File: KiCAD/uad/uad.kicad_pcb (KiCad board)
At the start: 2 copper layers, 100 x 70 mm, 58 parts, among them M3 ОтверстиеD3

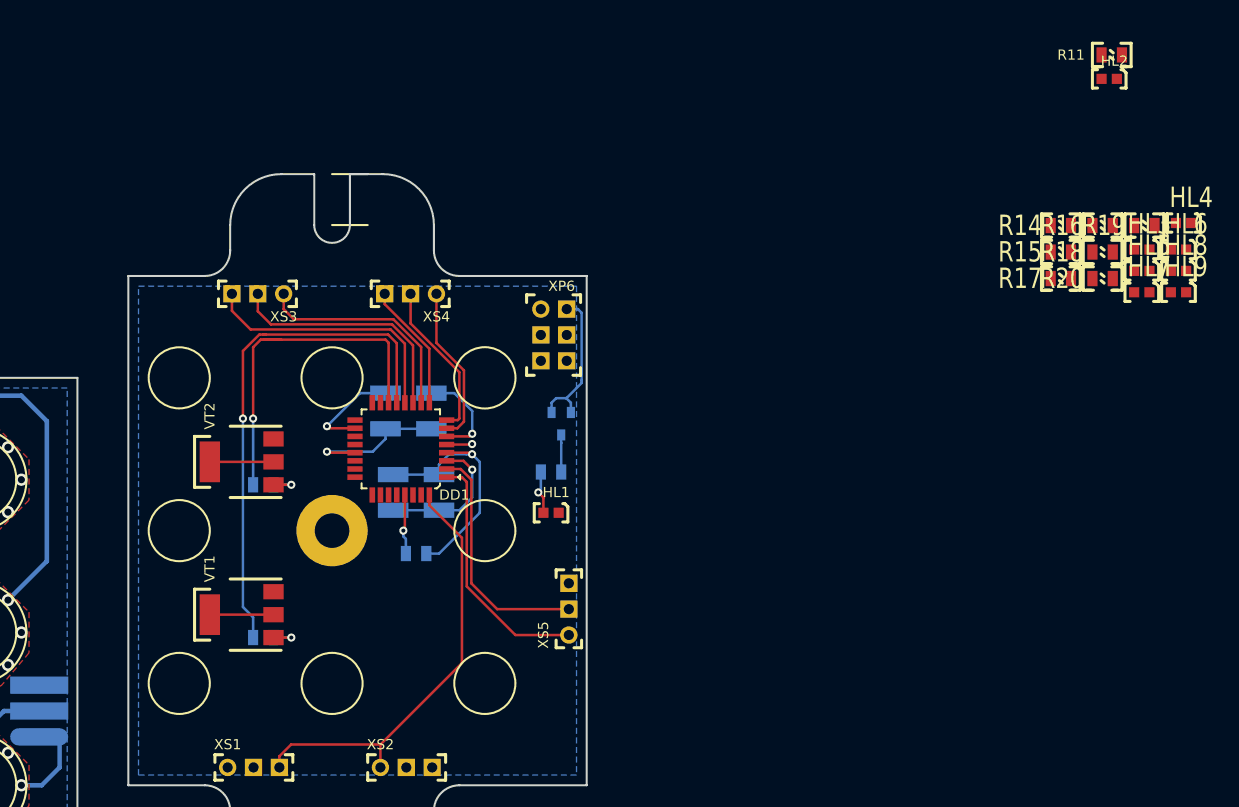
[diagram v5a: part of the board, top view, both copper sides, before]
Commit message: не поставлен эмиттерный повторитель на питание логики
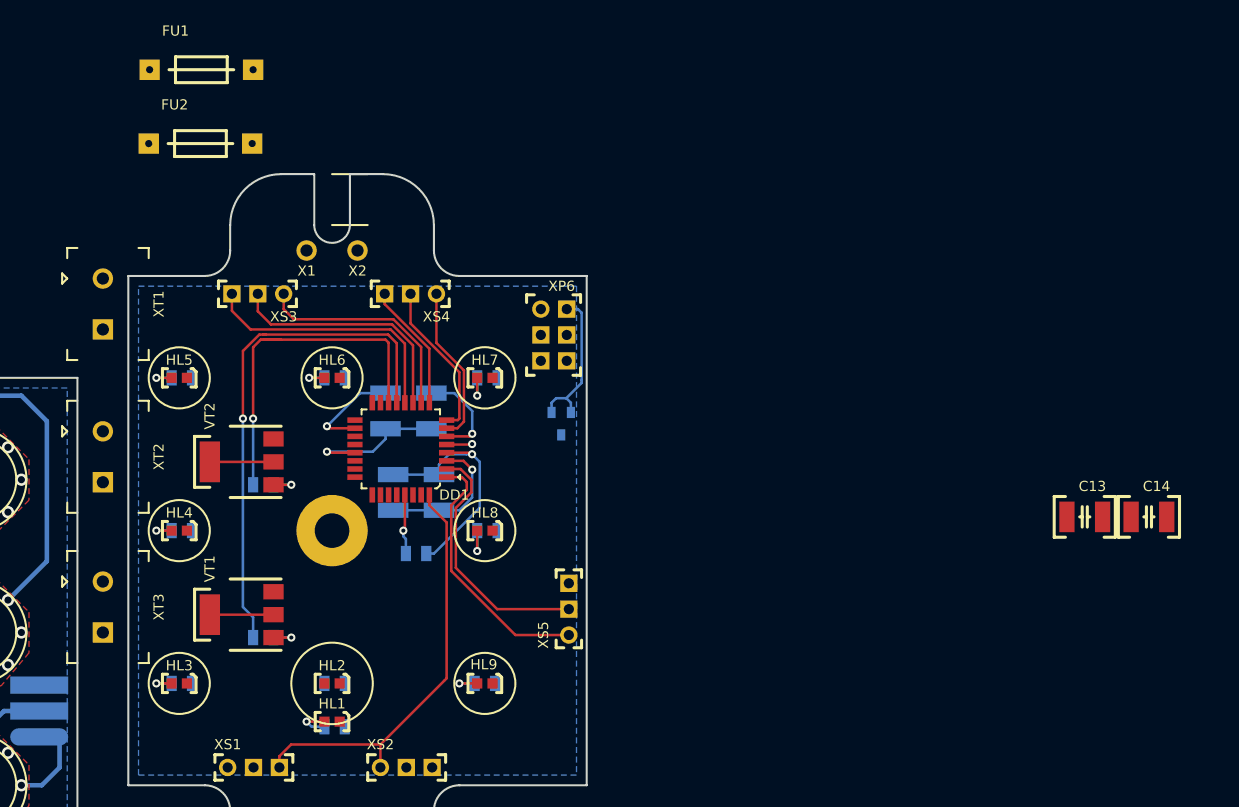
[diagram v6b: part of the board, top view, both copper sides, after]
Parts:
- added C13: 4.7мкФ(1210), N_RLC:Конденсатор_SMD_1210, F.Cu at (217.4, 111.7)
- added C14: 4.7мкФ(1210), N_RLC:Конденсатор_SMD_1210, F.Cu at (223.7, 111.7)
- added FU1: Предохранитель, N_RLC:Предохранитель_R700, F.Cu at (127.3, 67.8)
- added FU2: Предохранитель, N_RLC:Предохранитель_R700, F.Cu at (127.2, 75.0)
- added X1: L_220, N_X:ОтверстиеD1.2, F.Cu at (142.8, 85.5)
- added X2: N_220, N_X:ОтверстиеD1.2, F.Cu at (147.8, 85.5)
- added XT1: Клеммник_х2, N_X:Клеммник_х2_шаг5, F.Cu at (122.8, 88.2)
- added XT2: Клеммник_х2, N_X:Клеммник_х2_шаг5, F.Cu at (122.8, 103.2)
- added XT3: Клеммник_х2, N_X:Клеммник_х2_шаг5, F.Cu at (122.8, 118.0)
- R11, R14, R15, R16, R17, R18, R19, R20: moved to B.Cu
- moved HL3 103.7 mm to (129.5, 128.0)
- moved HL4 103.1 mm to (129.5, 113.0)
- moved HL2 96.7 mm to (144.5, 128.0)
- moved R11 96.6 mm to (146.5, 128.0), turned to 180 degrees
- moved R14 95.5 mm to (131.5, 128.0), turned to 180 degrees
- moved HL5 95.1 mm to (129.5, 98.0)
- moved R16 89.7 mm to (131.5, 98.0), turned to 180 degrees
- moved R15 88.6 mm to (131.5, 113.0), turned to 180 degrees
- moved HL6 84.0 mm to (144.5, 98.0)
- moved HL9 78.2 mm to (159.5, 128.0)
- moved HL8 72.7 mm to (159.5, 113.0)
- moved R20 70.9 mm to (161.2, 128.0), turned to 180 degrees
- moved R17 70.0 mm to (146.5, 98.0), turned to 180 degrees
- moved R19 69.3 mm to (161.5, 113.0), turned to 180 degrees
- moved HL7 65.0 mm to (159.5, 98.0)
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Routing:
- net Net-(HL8-Pad1): track 0.00 -> 4.00 mm, vias 0 -> 1
- net /uab_logic/VCC: track 47.9 -> 43.9 mm
- net Net-(HL7-Pad1): track 0.00 -> 3.50 mm, vias 0 -> 1
- net Net-(HL9-Pad1): track 0.00 -> 3.25 mm, vias 0 -> 1
- net Net-(HL6-Pad1): track 0.00 -> 3.00 mm, vias 0 -> 1
- net Net-(HL5-Pad1): track 0.00 -> 3.00 mm, vias 0 -> 1
- net Net-(HL4-Pad1): track 0.00 -> 3.00 mm, vias 0 -> 1
- net Net-(HL3-Pad1): track 0.00 -> 3.00 mm, vias 0 -> 1
- net /uab_logic/BUT_8_IN: track 24.4 -> 25.7 mm
- net /uab_logic/BUT_1_IN: track 23.7 -> 24.9 mm
- net /uab_logic/BUT_COM_OUT: track 42.9 -> 41.6 mm
- net Net-(HL1-Pad1): track 4.31 -> 3.71 mm

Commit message: обе схемы закончены, разводка второй платы не закончена
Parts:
- added C15: 4.7мкФ(1210), N_RLC:Конденсатор_SMD_1210, F.Cu at (198.0, 73.2)
- added G1: Стабилиатор_LM2931AZ-5.0G, N_G:Стабилизатор_корпус_TO-92, F.Cu at (233.1, 81.9)
- added L1: 33мкГн, N_RLC:Чип-индуктивность_SMD_0805, F.Cu at (231.5, 93.8)
- added L2: 33мкГн, N_RLC:Чип-индуктивность_SMD_0805, F.Cu at (247.2, 81.0)
- added L3: 33мкГн, N_RLC:Чип-индуктивность_SMD_0805, F.Cu at (242.5, 93.8)
- added VD2: Мост_DB155S, N_VD_HL:Диод_матрица_корпус_DB-1S, B.Cu at (153.2, 132.0)
- added VD3: Шоттки_BAR43CFILM, N_VD_HL:Диод_BAR43CFILM_SOT-23, F.Cu at (253.5, 89.8)
- added X3: L_12, N_X:ОтверстиеD1.2, F.Cu at (147.8, 140.0)
- added X4: N_12, N_X:ОтверстиеD1.2, F.Cu at (142.8, 140.0)
- FU1, FU2: footprint N_RLC:Предохранитель_R700 -> N_RLC:Предохранитель_MF-R_d10.4; moved to B.Cu
- VD1: value Диод_шоттки -> Шоттки_BAR43CFILM
- XT1, XT2, XT3: footprint N_X:Клеммник_х2_шаг5 -> N_X:Клеммник_х2_шаг2.54
- moved FU2 69.6 mm to (162.5, 135.0), turned to 45 degrees
- moved FU1 52.1 mm to (167.5, 101.0), turned to 90 degrees
- moved XT1 47.1 mm to (166.0, 107.0), turned to 90 degrees
- moved VD1 30.0 mm to (197.7, 101.6)
- moved XP6 29.8 mm to (195.5, 91.0)
- moved XT2 16.2 mm to (126.5, 119.0)
- moved XT3 14.0 mm to (126.5, 104.5)
- moved C1 10.2 mm to (95.2, 136.2)
- moved C2 10.2 mm to (80.2, 136.2)
- moved C3 10.2 mm to (80.2, 121.2)
- moved C4 10.2 mm to (80.2, 106.2)
- moved C5 10.2 mm to (95.2, 106.2)
- moved C6 10.2 mm to (110.2, 106.2)
- moved C8 10.2 mm to (110.2, 136.2)
- moved C7 10.1 mm to (110.2, 121.2)
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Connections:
- net Net-(FU1-Pad2) renamed /uab_logic/L2
- DD1 pad 1: /uab_logic/BUT_8_IN -> /uab_logic/LED_7
- DD1 pad 15: /uab_logic/MOSI -> /uab_logic/LED_5
- DD1 pad 16: /uab_logic/MISO -> /uab_logic/LED_4
- DD1 pad 2: /uab_logic/BUT_1_IN -> /uab_logic/LED_6
- DD1 pad 23: Net-(DD1-Pad23) -> /uab_logic/LED_3
- DD1 pad 24: Net-(DD1-Pad24) -> /uab_logic/LED_2
- DD1 pad 25: Net-(DD1-Pad25) -> /uab_logic/LED_1
- DD1 pad 26: Net-(DD1-Pad26) -> /uab_logic/BUT_COM_OUT
- DD1 pad 27: Net-(DD1-Pad27) -> /uab_logic/LED_8
- DD1 pad 28: Net-(DD1-Pad28) -> /uab_logic/BUT_8_IN
- DD1 pad 32: /uab_logic/BUT_COM_OUT -> /uab_logic/BUT_1_IN
- FU1 pad 1: Net-(FU1-Pad1) -> /uab_logic/L1
- FU2 pad 1: Net-(FU2-Pad1) -> /uab_logic/L1_12
- FU2 pad 2: Net-(FU2-Pad2) -> /uab_logic/L2_12
- X2 pad 1: Net-(FU2-Pad2) -> /uab_logic/N1
- XP6 pad 1: /uab_logic/MISO -> /uab_logic/LED_4
- XP6 pad 4: /uab_logic/MOSI -> /uab_logic/LED_5
- XT1 pad 1: Net-(FU1-Pad1) -> /uab_logic/N1
- XT1 pad 2: Net-(FU2-Pad1) -> /uab_logic/L1
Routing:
- net /uab_logic/N1: track 0.00 -> 41.5 mm
- net /uab_logic/LED_2: track 0.00 -> 34.1 mm, vias 0 -> 1
- net /uab_logic/N1_12: track 0.00 -> 27.5 mm
- net /uab_logic/PWM_OUT_1: track 50.8 -> 24.1 mm
- net /uab_logic/L2: track 0.00 -> 24.4 mm
- net /uab_logic/LED_8: track 0.00 -> 21.6 mm, vias 0 -> 1
- net /uab_logic/LED_1: track 0.00 -> 20.0 mm, vias 0 -> 1
- net /uab_logic/LED_4: track 0.00 -> 19.9 mm, vias 0 -> 1
- net /uab_logic/LED_3: track 0.00 -> 18.5 mm, vias 0 -> 1
- net /uab_logic/L1_12: track 0.00 -> 16.8 mm
- net /uab_logic/LED_6: track 0.00 -> 16.7 mm, vias 0 -> 1
- net Net-(VD1-Pad1): track 14.8 -> 0.00 mm
- net /uab_logic/PWM_OUT_2: track 34.9 -> 22.1 mm
- net /uab_logic/LED_7: track 0.00 -> 11.2 mm, vias 0 -> 1
- net /uab_logic/LED_5: track 0.00 -> 5.66 mm, vias 0 -> 1
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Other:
- outline, holes or cut-outs redrawn
- net class power added: clearance 0.4, trace_width 0.45, via_dia 0.8, via_drill 0.4

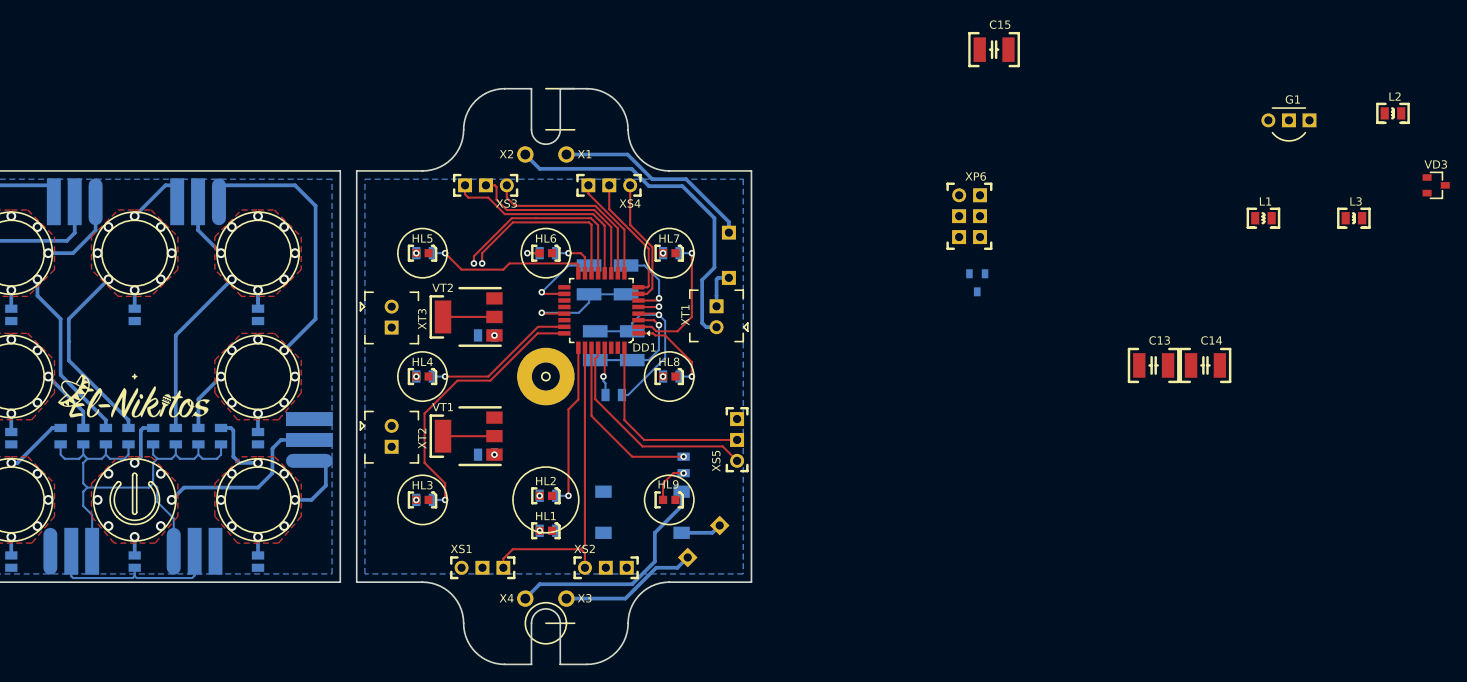
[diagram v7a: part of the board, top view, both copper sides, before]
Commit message: закончена разводка первого варианта (без отскока) и без фрезеровки
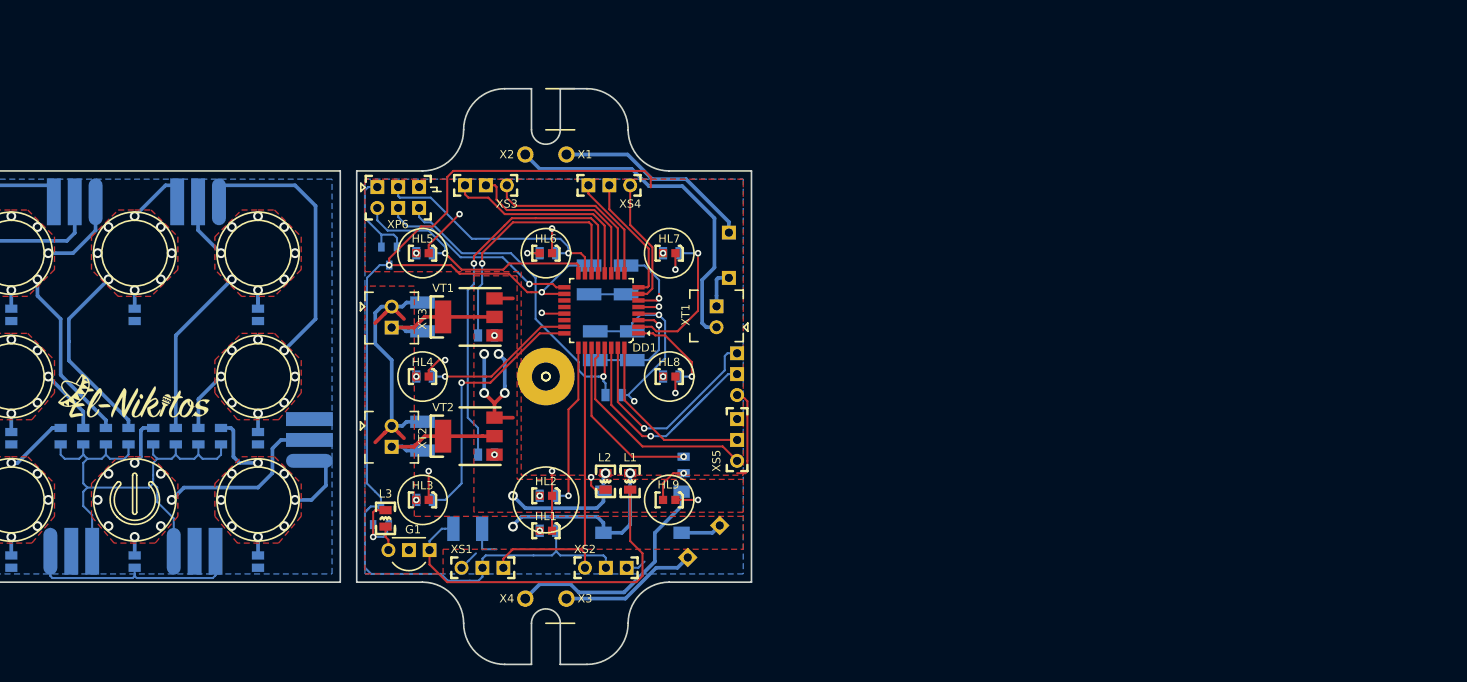
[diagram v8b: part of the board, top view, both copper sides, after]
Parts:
- removed the R12 at (139.0, 122.5)
- added R13: 300 Ом(0805), N_RLC:Резистор_SMD_0805_0,125Вт, B.Cu at (139.0, 122.5)
- added XP7: Вилка_PLS3, N_X:Вилка_PLS3_вертикальная, B.Cu at (168.5, 115.2)
- C13, C14, C15, VD3: moved to B.Cu
- moved VD3 134.4 mm to (125.2, 129.9), turned to 90 degrees
- moved L3 122.6 mm to (125.8, 131.2), turned to 90 degrees
- moved G1 119.1 mm to (126.1, 134.1)
- moved L2 104.4 mm to (152.5, 124.8), turned to 270 degrees
- moved C14 93.5 mm to (130.2, 107.5), turned to 90 degrees
- moved C13 87.8 mm to (130.2, 122.0), turned to 90 degrees
- moved C15 84.0 mm to (137.5, 131.5), turned to 180 degrees
- moved L1 82.1 mm to (155.5, 124.8), turned to 270 degrees
- moved VD1 71.6 mm to (126.2, 98.3)
- moved XP6 70.8 mm to (124.8, 92.5), turned to 0 degrees
- renumbered R13 to R12, VT2 to VT1, VT1 to VT2
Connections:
- C13 pad 1: Net-(C13-Pad1) -> /uab_logic/collector_2
- C14 pad 1: Net-(C14-Pad1) -> /uab_logic/collector_1
- DD1 pad 13: /uab_logic/PWM_OUT_1 -> /uab_logic/PWM_OUT_2
- DD1 pad 14: /uab_logic/PWM_OUT_2 -> /uab_logic/PWM_OUT_1
- R12 pad 2: /uab_logic/PWM_OUT_2 -> /uab_logic/PWM_OUT_1
- VT1 pad 2: Net-(C13-Pad1) -> /uab_logic/collector_1
- VT1 pad 4: Net-(C13-Pad1) -> /uab_logic/collector_1
- VT2 pad 2: Net-(C14-Pad1) -> /uab_logic/collector_2
- VT2 pad 4: Net-(C14-Pad1) -> /uab_logic/collector_2
- XP1 pad 2: /uad_sensor/GND -> /uad_sensor/VCC_1
- XP2 pad 2: /uad_sensor/GND -> /uad_sensor/VCC_2
- XS1 pad 2: /uab_logic/GND -> /uab_logic/VCC
- XS2 pad 2: /uab_logic/GND -> /uab_logic/VCC
- XT2 pad 2: Net-(C13-Pad1) -> /uab_logic/collector_2
- XT3 pad 2: Net-(C14-Pad1) -> /uab_logic/collector_1
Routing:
- net /uab_logic/VCC: track 43.9 -> 184.8 mm, vias 3 -> 5
- net /uab_logic/PWR_12V: track 0.00 -> 57.7 mm, vias 0 -> 2
- net /uab_logic/GND: track 31.1 -> 77.2 mm, vias 3 -> 12
- net Net-(C15-Pad2): track 0.00 -> 44.6 mm
- net /uab_logic/PWR_GND: track 0.00 -> 35.1 mm, vias 0 -> 6
- net /uab_logic/RES: track 5.92 -> 41.0 mm
- net /uab_logic/RX: track 0.00 -> 32.8 mm, vias 0 -> 1
- net /uab_logic/TX: track 0.00 -> 27.2 mm, vias 0 -> 1
- net /uab_logic/PWM_OUT_2: track 22.1 -> 48.2 mm
- net /uab_logic/LED_5: track 5.66 -> 30.8 mm
- net /uab_logic/SCK: track 0.00 -> 24.9 mm, vias 0 -> 1
- net /uab_logic/collector_2: track 0.00 -> 17.0 mm
- net /uab_logic/collector_1: track 0.00 -> 17.0 mm
- net Net-(VD1-Pad1): track 0.00 -> 12.5 mm
- net /uab_logic/LED_4: track 19.9 -> 31.8 mm
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- added copper zone on F.Cu, net /uab_logic/PWR_12V
- added copper zone on F.Cu, net /uab_logic/PWR_GND
- added copper zone on F.Cu, net /uab_logic/VCC
